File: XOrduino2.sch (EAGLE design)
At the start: 83 parts, among them J1 10x1F-H8.5, J2 8x1F-H8.5, J3 8x1F-H8.5, J4 6x1F-H8.5, J5 2.5mm, J6 2.5mm, J7 2.5mm, J8 2.5mm, P1 10k, Q1 TEMT6000, SW3 LEFT BUMPER, SW4 RIGHT BUMPER, U1 ATMEGA32U4-XUAU, U2 LMV358, U3 NJU7261, U4 DRV8833PWP, U5 QRE1113GR, U6 QRE1113GR, X1 USBPCB, X2 USBMINIB, Y1 16MHz

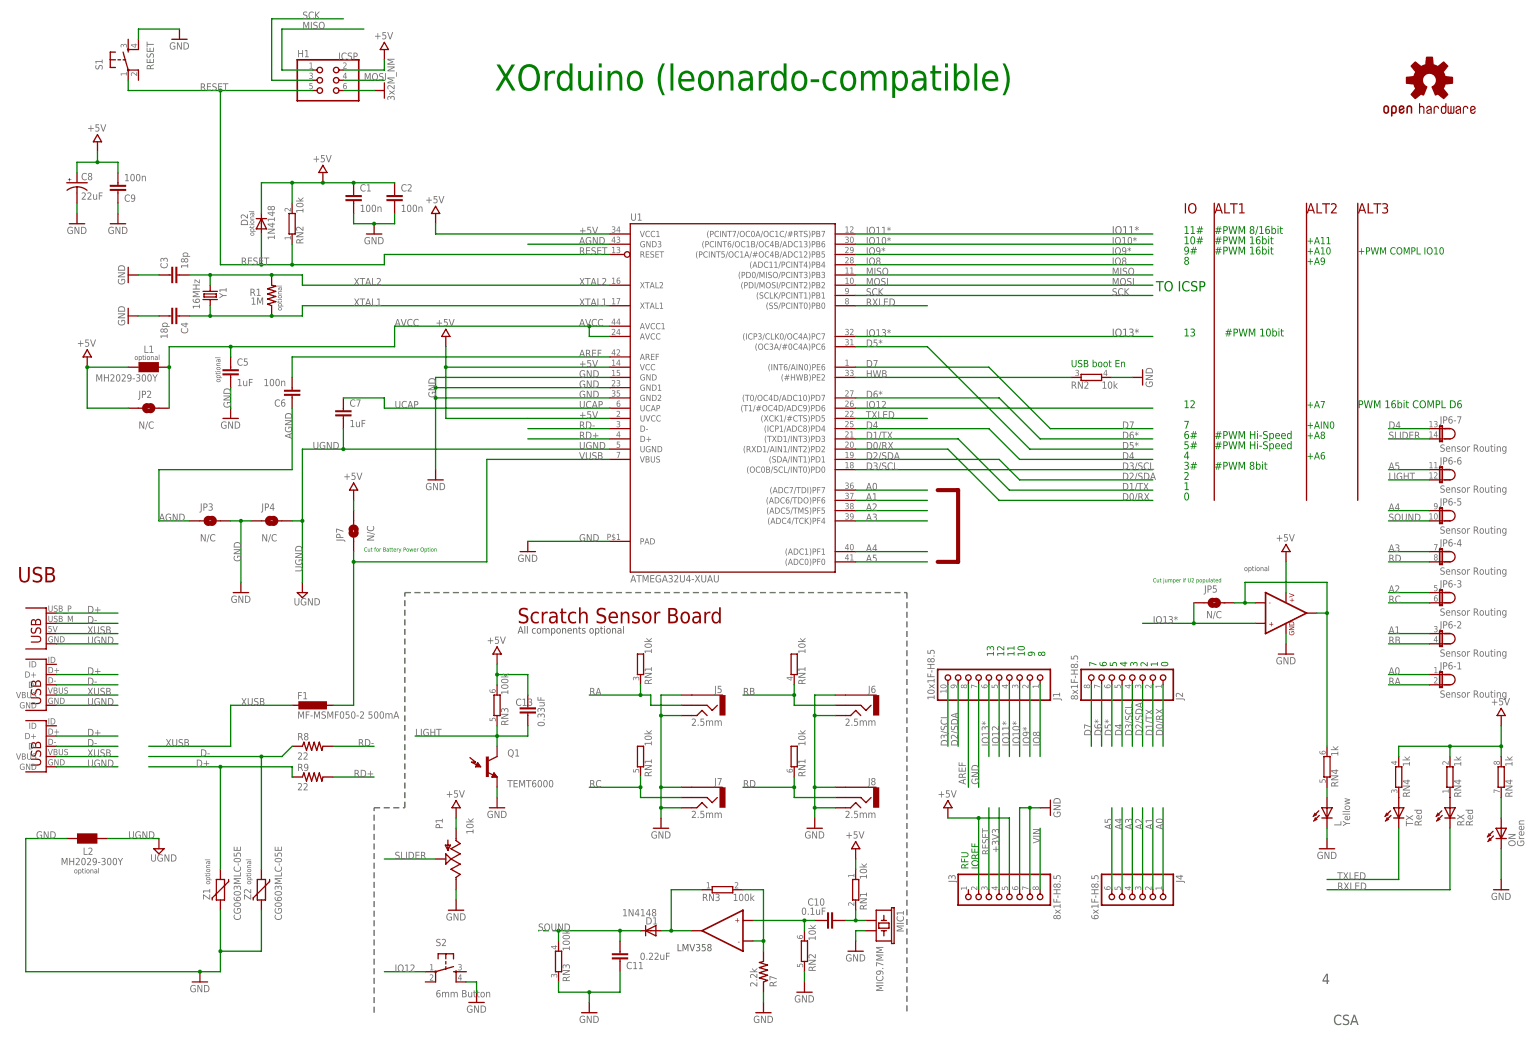
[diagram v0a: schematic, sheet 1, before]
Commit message: First version of Xorduino2 (v5) board w/ all components placed.
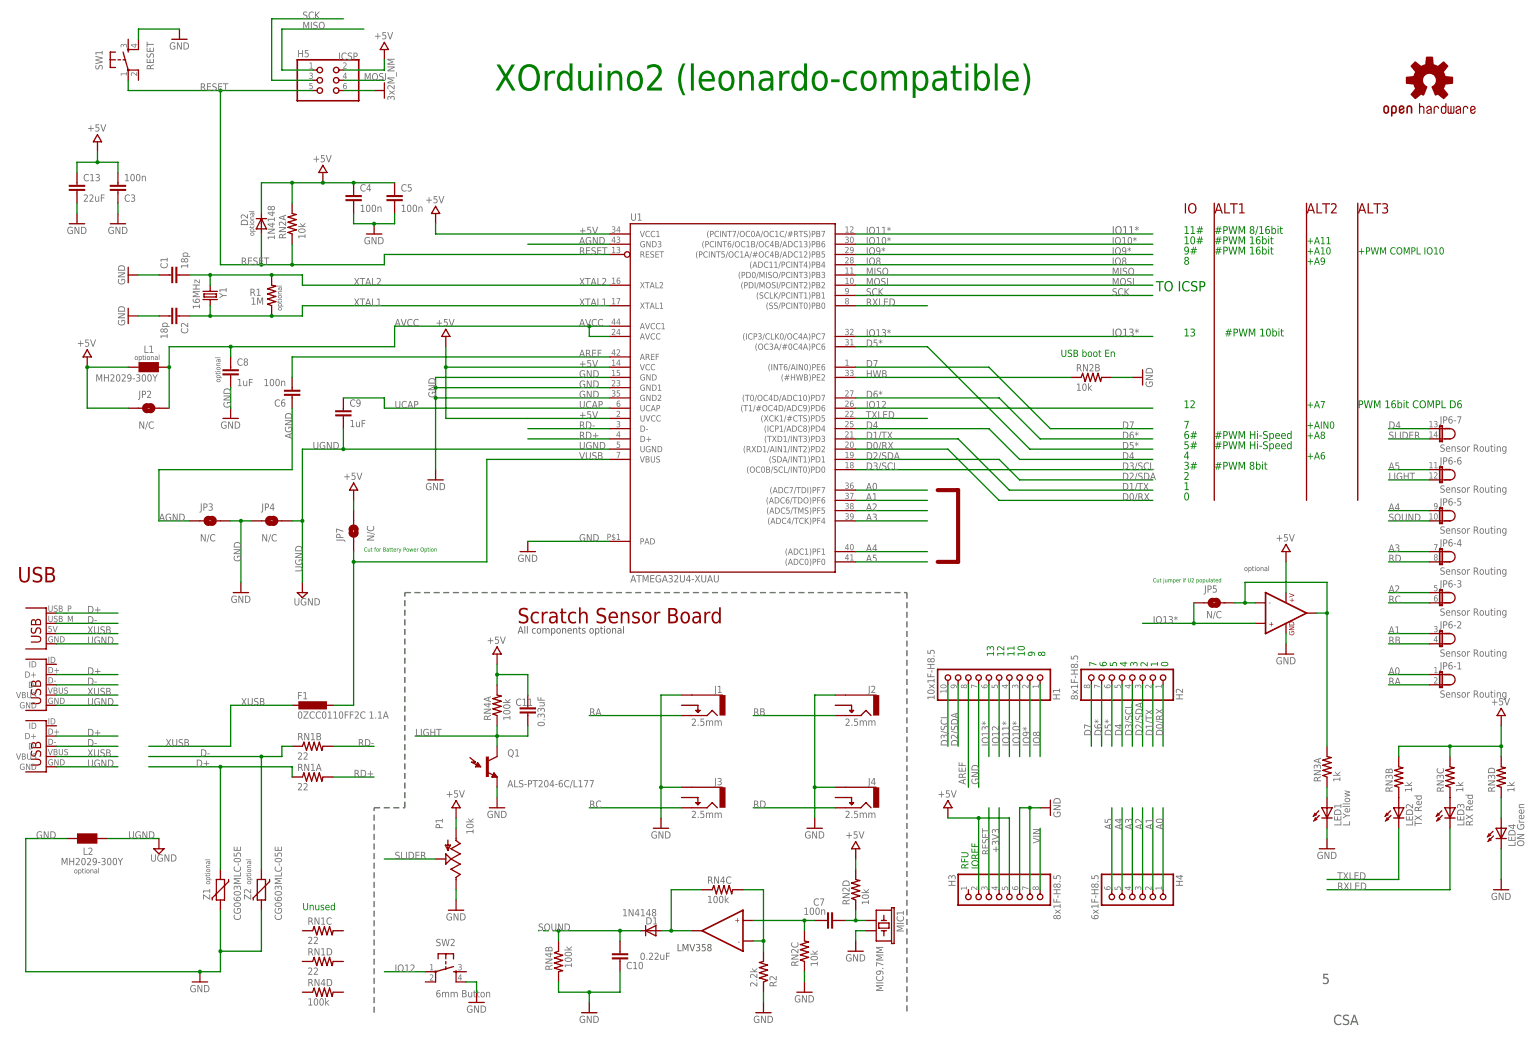
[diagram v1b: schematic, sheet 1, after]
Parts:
- removed D5: 1N4148, SparkFun-DiscreteSemi:DIODE1N4148
- removed FAULT: Red, led:LED3MM
- removed J8: 2.5mm, SparkFun:AUDIO-JACKSMD
- removed JP13: MOT L, SparkFun:M023.5MM
- removed JP14: MOT R, SparkFun:M023.5MM
- removed JP8: (no value), SparkFun-Connectors:M02PTH
- removed R10, R6: 220, SparkFun-Passives:RESISTORAXIAL-0.3
- removed R11, R12: 100k, SparkFun-Passives:RESISTORAXIAL-0.3
- removed R4, R5: 400m 1/8W, SparkFun-Passives:RESISTORAXIAL-0.3
- removed R7: 2.2k, SparkFun-Passives:RESISTORAXIAL-0.3
- removed R8, R9: 22, SparkFun-Passives:RESISTORAXIAL-0.3
- added D4: 1A Schottkey, SparkFun-DiscreteSemi:DIODE-SCHOTTKY_
- added H2, H3: 8x1F-H8.5, SmartPrj:PINHD-1X8
- added H4: 6x1F-H8.5, SmartPrj:PINHD-1X6
- added H5: ICSP, SmartPrj:PINHD-2X3
- added LED5: FAULT Red, led:LED3MM
- added RN5: 100k, xorduino:RESISTOR-ARRAYCRA06S
- added RN6: 220, xorduino:RESISTOR-ARRAYCRA06S
- added RN7: 1ohm 1/16W, resistor-dil:4R-NEXB38V
- C1, C2: value 100n -> 18p; device SparkFun-Passives:CAPPTH -> SparkFun-Passives:CAP0805
- C10: value 0.1uF -> 0.22uF; device SparkFun-Passives:CAPPTH -> SparkFun-Passives:CAP0805
- C11: value 0.22uF -> 0.33uF; device SparkFun-Passives:CAPPTH -> SparkFun-Passives:CAP0805
- C12: value 0.01uF -> 10uF; device SparkFun-Passives:CAPPTH -> SparkFun-Passives:CAP0805
- C13: value 0.33uF -> 22uF; device SparkFun-Passives:CAPPTH -> SparkFun-Passives:CAP1206
- C14: value 10uF -> 22uF; device SparkFun-Passives:CAP_POLPTH2 -> SparkFun-Passives:CAP1206
- C15: value 22uF -> 0.01uF; device SparkFun-Passives:CAP_POLPTH2 -> SparkFun-Passives:CAP0805
- C3, C4: value 18p -> 100n; device SparkFun-Passives:CAPPTH -> SparkFun-Passives:CAP0805
- C5, C7: value 1uF -> 100n; device SparkFun-Passives:CAPPTH -> SparkFun-Passives:CAP0805
- C6: device SparkFun-Passives:CAPPTH -> SparkFun-Passives:CAP0805
- C8: value 22uF -> 1uF; device SparkFun-Passives:CAP_POLPTH2 -> SparkFun-Passives:CAP0805
- C9: value 100n -> 1uF; device SparkFun-Passives:CAPPTH -> SparkFun-Passives:CAP0805
- D3: value 1N4148 -> 1A Schottkey; device SparkFun-DiscreteSemi:DIODE1N4148 -> SparkFun-DiscreteSemi:DIODE-SCHOTTKY_
- F1: value MF-MSMF050-2 500mA -> 0ZCC0110FF2C 1.1A
- H1: value ICSP -> 10x1F-H8.5; device SmartPrj:PINHD-2X3 -> SmartPrj:PINHD-1X10
- J1: value 10x1F-H8.5 -> 2.5mm; device SmartPrj:PINHD-1X10 -> xorduino:AUDIO-JACK
- J2, J3: value 8x1F-H8.5 -> 2.5mm; device SmartPrj:PINHD-1X8 -> xorduino:AUDIO-JACK
- J4: value 6x1F-H8.5 -> 2.5mm; device SmartPrj:PINHD-1X6 -> xorduino:AUDIO-JACK
- J5: value 2.5mm -> Batt In; device SparkFun:AUDIO-JACKSMD -> SparkFun-Connectors:M02PTH
- J6: value 2.5mm -> MOT L; device SparkFun:AUDIO-JACKSMD -> SparkFun:M023.5MM
- J7: value 2.5mm -> MOT R; device SparkFun:AUDIO-JACKSMD -> SparkFun:M023.5MM
- LED1: value Yellow -> L Yellow
- LED2: value Red -> TX Red
- LED3: value Red -> RX Red
- LED4: value Green -> ON Green
- Q1: value TEMT6000 -> ALS-PT204-6C/L177; device SparkFun:TEMT6000 -> xorduino:ALS-PT204-6C/L177
- R1, R3: device SparkFun-Passives:RESISTORAXIAL-0.3 -> SparkFun-Passives:RESISTOR0805-RES
- R2: value 20k-75k -> 2.2k; device SparkFun-Passives:RESISTORAXIAL-0.3 -> SparkFun-Passives:RESISTOR0805-RES
- RN1: value 10k -> 22; device resistor-sil:GE05RP -> xorduino:RESISTOR-ARRAYCRA06S
- RN2: device resistor-sil:E3RP -> xorduino:RESISTOR-ARRAYCRA06S
- RN3: value 100k -> 1k; device resistor-sil:E3RP -> xorduino:RESISTOR-ARRAYCRA06S
- RN4: value 1k -> 100k; device resistor-sil:E4RP -> xorduino:RESISTOR-ARRAYCRA06S
- renumbered L to LED1, ON to LED4, RX to LED3, S1 to SW1, S2 to SW2, TX to LED2, U$16 to X3
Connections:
- removed net N$21: R5.2, U4.AISEN
- new net N$20: RN7A.1, RN7B.1, U4.AISEN
- net +3V3: now also H3.4; no longer J3.4
- net +5V: now also C11.1, C3.2, C4.1, C5.1, H3.2, H3.5, H5.2, RN2D.2, RN3B.2, RN3D.2, RN5A.2, RN5B.2; no longer C1.1, C2.1, C8.+, C9.2, H1.2, J3.2, J3.5, R11.1, R12.1, RN1A.1, RN4B.2, RN4D.2
- net A0: now also H4.1; no longer J4.1
- net A1: now also H4.2; no longer J4.2
- net A2: now also H4.3; no longer J4.3
- net A3: now also H4.4; no longer J4.4
- net A4: now also H4.5; no longer J4.5
- net A5: now also H4.6; no longer J4.6
- net AREF: now also H1.8; no longer J1.8
- net AVCC: now also C8.1; no longer C5.1
- net D+: now also RN1A.1; no longer R9.1
- net D-: now also RN1B.1; no longer R8.1
- net D0/RX: now also H2.1; no longer J2.1
- net D1/TX: now also H2.2; no longer J2.2
- net D2/SDA: now also H1.9, H2.3; no longer J1.9, J2.3
- net D3/SCL: now also H1.10, H2.4; no longer J1.10, J2.4
- net D4: now also H2.5; no longer J2.5
- net D5*: now also H2.6; no longer J2.6
- net D6*: now also H2.7; no longer J2.7
- net D7: now also H2.8; no longer J2.8
- net GND: now also C1.1, C10.1, C12.2, C13.2, C14.2, C8.2, H1.7, H3.6, H3.7, H5.6, J1.SLEEVE, J2.SLEEVE, J3.SLEEVE, J4.SLEEVE, J5.2, R2.1, RN4B.2, RN7A.2, RN7B.2, RN7C.2, RN7D.2; no longer C1.2, C11.1, C14.-, C15.-, C8.-, C9.1, H1.6, J1.7, J3.6, J3.7, J5.1, J5.5, J6.1, J6.5, J7.1, J7.5, J8.1, J8.5, JP8.2, R4.1, R5.1, R7.1, RN3B.1
- net IO10*: now also H1.3; no longer J1.3
- net IO11*: now also H1.4; no longer J1.4
- net IO12: now also H1.5; no longer J1.5
- net IO13*: now also H1.6; no longer J1.6
- net IO8: now also H1.1, RN5A.1; no longer J1.1, R11.2
- net IO9*: now also H1.2, RN5B.1; no longer J1.2, R12.2
- net LIGHT: now also C11.2, RN4A.1; no longer C13.2, RN3C.1
- net MISO: now also H5.1; no longer H1.1
- net MOSI: now also H5.4; no longer H1.4
- net MOTL+: now also J6.1; no longer JP13.1
- net MOTL-: now also J6.2; no longer JP13.2
- net MOTR+: now also J7.2; no longer JP14.2
- net MOTR-: now also J7.1; no longer JP14.1
- net N$1: now also LED3.A, RN3C.1; no longer LED2.A, RN4B.1
- net N$10: now also C12.1; no longer C14.+
- net N$11: now also C7.2; no longer C10.2
- net N$12: now also LED5.C; no longer FAULT.C
- net N$13: now also RN6B.2; no longer R10.1
- net N$15: now also RN6A.2; no longer R6.1
- net N$16: now also RN4C.1; no longer RN3A.1
- net N$17: now also D4.A, J5.1; no longer D3.A, JP8.1
- net N$18: now also LED5.A; no longer FAULT.A
- net N$19: now also RN7C.1, RN7D.1; no longer R4.2
- net N$2: now also RN3A.1; no longer RN4C.1
- net N$3: now also RN3D.1; no longer RN4D.1
- net N$4: now also LED2.A, RN3B.1; no longer LED3.A, RN4A.1
- net N$5: now also R2.2, RN4C.2; no longer R7.2, RN3A.2
- net N$6: now also RN3A.2; no longer RN4C.2
- net N$7: now also C15.1; no longer C12.1
- net N$8: now also RN5C.2, RN5D.2; no longer R2.1
- net N$9: now also C7.1, RN2D.1; no longer C10.1, RN1A.2
- net RA: now also J1.TIP; no longer J5.2, RN1B.2
- net RB: now also J2.TIP; no longer J6.2, RN1C.2
- net RC: now also J3.TIP; no longer J7.2, RN1D.2
- net RD: now also J4.TIP; no longer J8.2, RN1E.2
- net RD+: now also RN1A.2; no longer R9.2
- net RD-: now also RN1B.2; no longer R8.2
- net RESET: now also H3.3, H5.5; no longer H1.5, J3.3
- net SCK: now also H5.3; no longer H1.3
- net SOUND: now also C10.2, RN4B.1; no longer C11.2, RN3B.2
- net UCAP: now also C9.1; no longer C7.1
- net UGND: now also C9.2; no longer C7.2
- net VIN: now also C14.1, C15.2, D4.C, H3.8, RN5C.1, RN5D.1, RN6A.1, RN6B.1; no longer C12.2, C15.+, D5.C, J3.8, R10.2, R2.2, R6.2
- net VUSB: now also D3.A; no longer D5.A
- net XTAL1: now also C2.1; no longer C4.1
- net XTAL2: now also C1.2; no longer C3.2
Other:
- note added: "2.6V minimum VM"
- note added: "Imax=200mV/R"
- note added: "Must be 20k-75k"
- note added: "Pmax=Imax^2*R"
- note added: "Unused"
- note added: "X7R ceramic 16V"
- note added: "XOrduino2 (leonardo-compatible)"
- note added: "w/ Vf = .5V @ 1A, min Vin = 3.1 => 3 cells @ 1.03V"
- note added: "w/ Vf = .9V @ 1A, min Vin = 3.5 => 3 cells @ 1.17V"
- note removed: "Batt In"
- note removed: "Imax=200mV/R4"
- note removed: "Imax=200mV/R5"
- note removed: "Pmax=Imax^2*R4"
- note removed: "Pmax=Imax^2*R5"
- note removed: "XOrduino (leonardo-compatible)"
- note removed: "XXX: use resistor arrays"
- moved on the sheet: C1, C10, C11, C12, C13, C2, C3, C4, C5, C7, C9, JP1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

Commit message: 70% 2-layer routed version of XOrduino2.
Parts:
- J6: value MOT L -> MOT R
- J7: value MOT R -> MOT L
- JP1, JP2, JP3, JP4, JP5, JP7: device SparkFun-Passives:SOLDERJUMPERTRACE -> xorduino:SOLDERJUMPERNOCONFLICT
- JP6: device xorduino:JP7QES -> xorduino:JP7QESNOCONFLICT
- SW3: device xorduino:SWITCH-SPDTV1 -> xorduino:SWITCH-SPDTV1-NOHOLES
- SW4: device xorduino:SWITCH-SPDTV2 -> xorduino:SWITCH-SPDTV2-NOHOLES
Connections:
- net +5V: now also P1.E, RN4D.2, RN5A.1, RN5B.1; no longer P1.A, RN4A.2, RN5A.2, RN5B.2
- net D+: now also RN1B.2; no longer RN1A.1
- net D-: now also RN1C.2; no longer RN1B.1
- net GND: now also P1.A; no longer P1.E
- net IO8: now also RN5A.2; no longer RN5A.1
- net IO9*: now also RN5B.2; no longer RN5B.1
- net LIGHT: now also RN4D.1; no longer RN4A.1
- net MOTL+: now also J7.2, U4.BOUT1; no longer J6.1, U4.AOUT1
- net MOTL-: now also J7.1, U4.BOUT2; no longer J6.2, U4.AOUT2
- net MOTR+: now also J6.1, U4.AOUT1; no longer J7.2, U4.BOUT1
- net MOTR-: now also J6.2, U4.AOUT2; no longer J7.1, U4.BOUT2
- net N$12: now also R3.2; no longer LED5.C
- net N$18: now also LED5.C, R3.1; no longer LED5.A, R3.2
- net RD+: now also RN1B.1; no longer RN1A.2
- net RD-: now also RN1C.1; no longer RN1B.2
- net VIN: now also LED5.A; no longer R3.1
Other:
- note added: "A"
- note added: "B"
- note added: "C"
- note added: "D"
- moved on the sheet: LED5, P1, R3, RN1A, RN1B, RN1C, RN4A, RN4D, RN5A, RN5B, U3

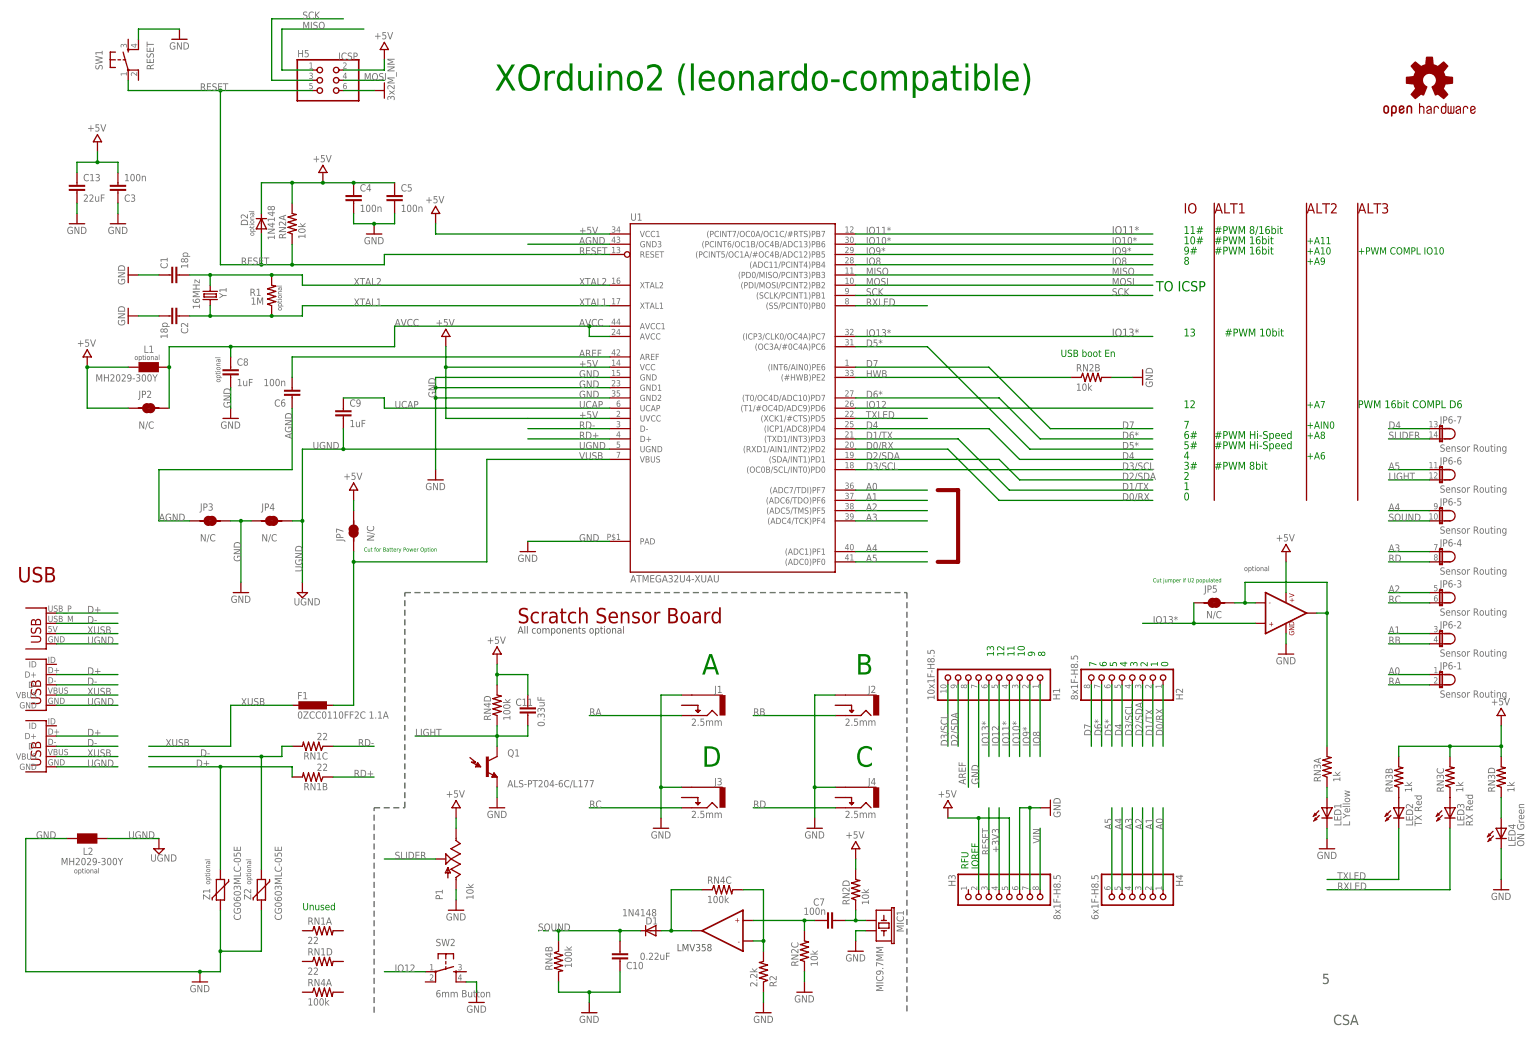
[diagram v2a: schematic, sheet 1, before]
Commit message: Almost-completely 4-layer routed version of XOrduino2.
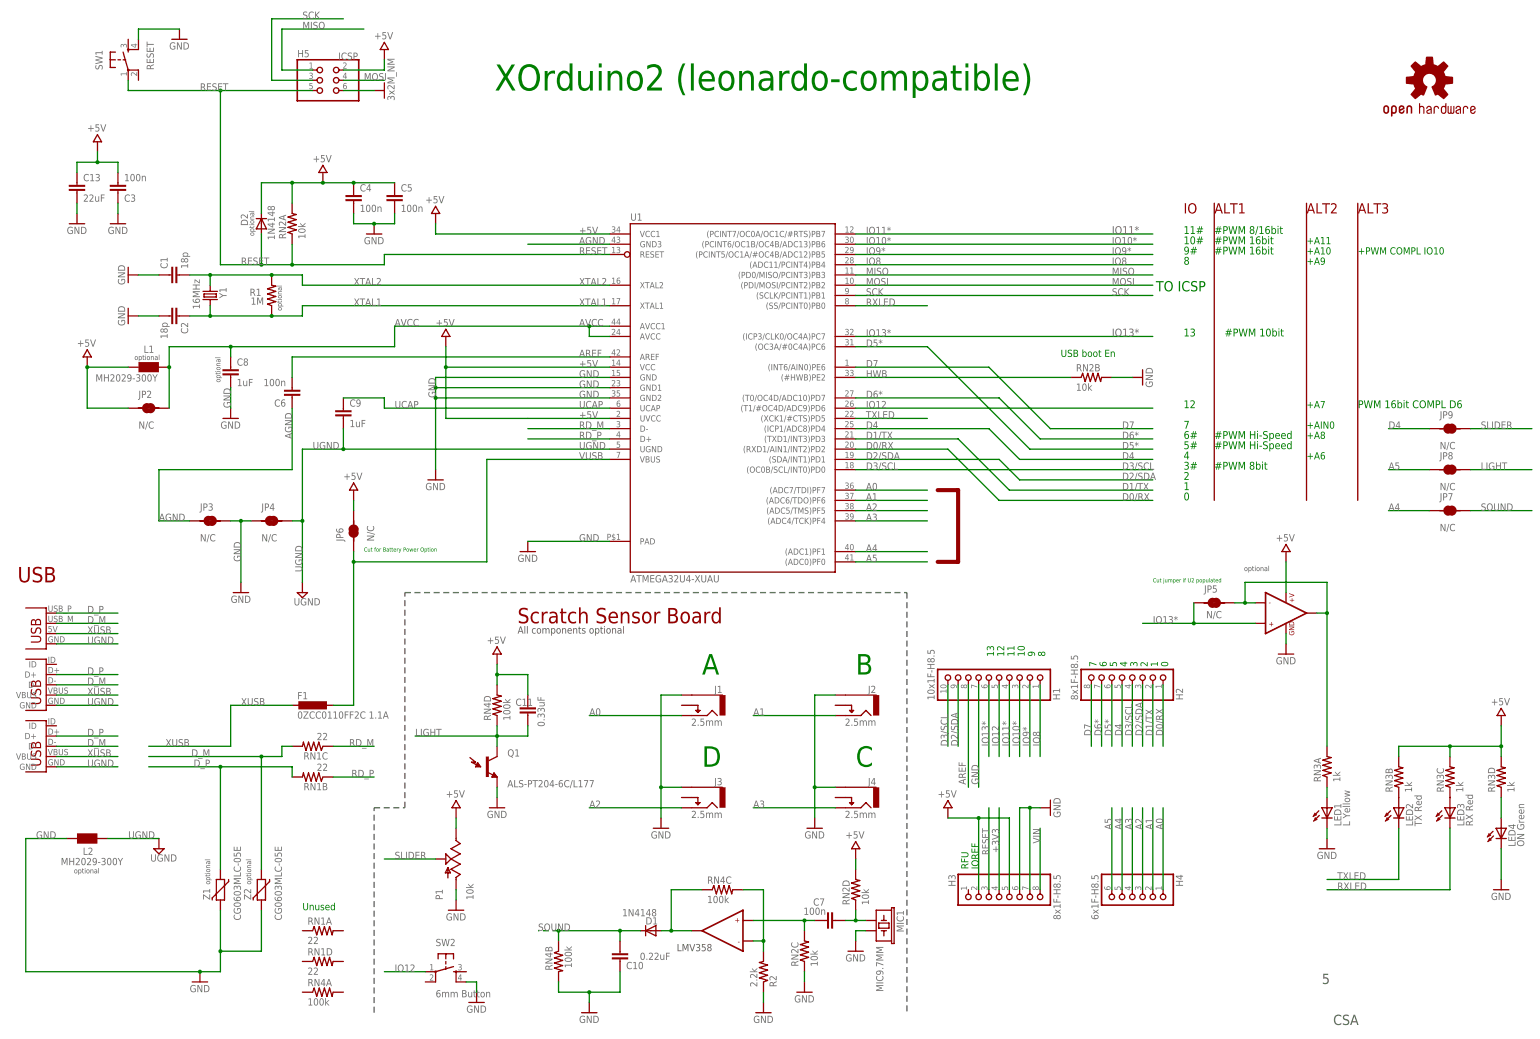
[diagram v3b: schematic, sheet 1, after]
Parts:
- added JP10, JP11, JP8, JP9: N/C, xorduino:SOLDERJUMPERBOT-NOCONFLICT
- JP1, JP7: device xorduino:SOLDERJUMPERNOCONFLICT -> xorduino:SOLDERJUMPERBOT-NOCONFLICT
- JP6: value Sensor Routing -> N/C; device xorduino:JP7QESNOCONFLICT -> xorduino:SOLDERJUMPERNOCONFLICT
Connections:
- net D+ renamed D_P
- net D- renamed D_M
- net RD+ renamed RD_P
- net RD- renamed RD_M
- removed net RA: J1.TIP, JP6-1.2
- removed net RB: J2.TIP, JP6-2.2
- removed net RC: J3.TIP, JP6-3.2
- removed net RD: J4.TIP, JP6-4.2
- new net N$21: JP10.1, RN5A.2, U5.C
- new net N$22: JP11.1, RN5B.2, U6.C
- net +5V: now also JP6.2; no longer JP7.2
- net A0: now also J1.TIP; no longer JP6-1.1
- net A1: now also J2.TIP; no longer JP6-2.1
- net A2: now also J3.TIP; no longer JP6-3.1
- net A3: now also J4.TIP; no longer JP6-4.1
- net A4: now also JP7.1; no longer JP6-5.1
- net A5: now also JP8.1; no longer JP6-6.1
- net D4: now also JP9.1; no longer JP6-7.1
- net IO8: now also JP10.2; no longer RN5A.2, U5.C
- net IO9*: now also JP11.2; no longer RN5B.2, U6.C
- net LIGHT: now also JP8.2; no longer JP6-6.2
- net SLIDER: now also JP9.2; no longer JP6-7.2
- net SOUND: now also JP7.2; no longer JP6-5.2
- net VUSB: now also JP6.1; no longer JP7.1
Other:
- moved on the sheet: JP7
